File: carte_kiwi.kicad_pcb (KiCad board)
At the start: 2 copper layers, 50 x 50 mm, 44 parts, among them IC1 MCP2562, P1 CONN_01X05, P2 CONN_01X03, P3 CONN_01X05, P4 CONN_01X03, P5 Serial Wire, P6 CAN_conn, P7 CONN_01X03, P8 CONN_01X03, P9 CAN_conn, SW1 SW_Push, U1 LD1117S50TR, U2 LD1117S33TR, U3 STM32F303K8

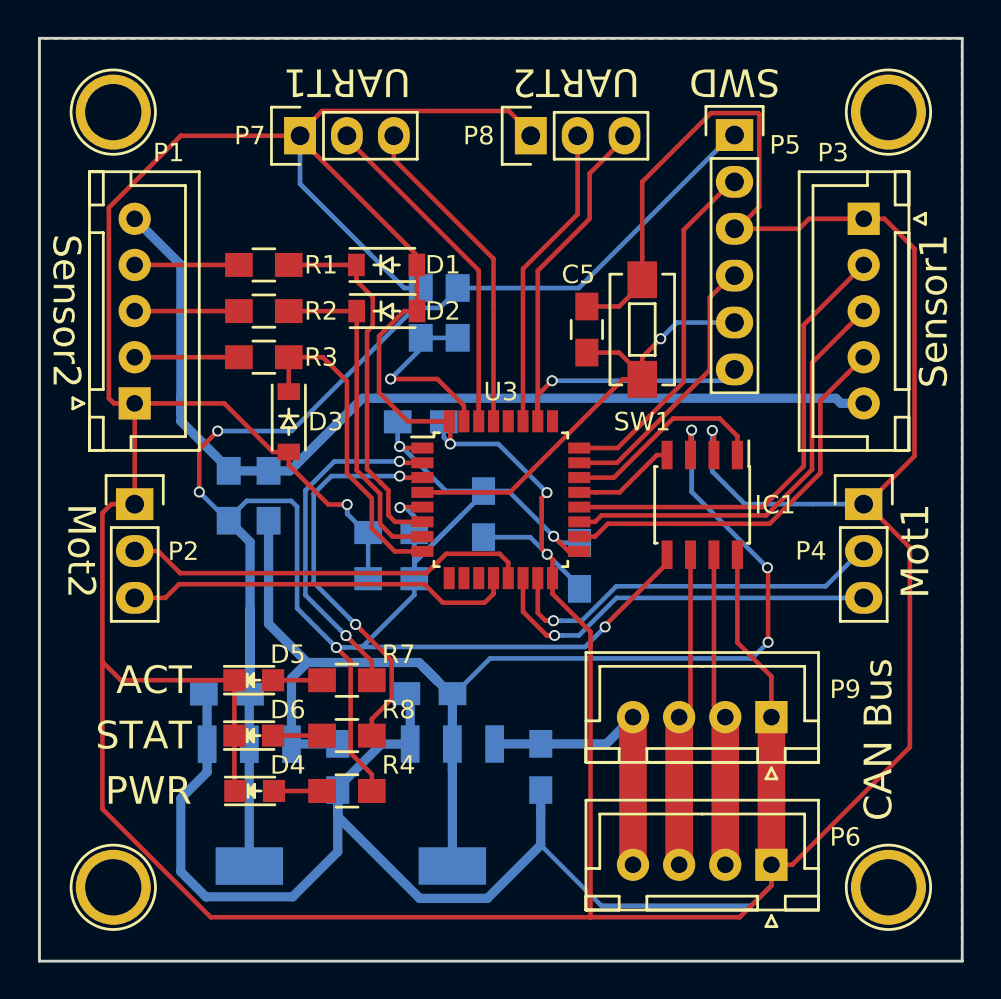
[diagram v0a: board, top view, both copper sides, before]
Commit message: ajoute via de connection entre plans de masse
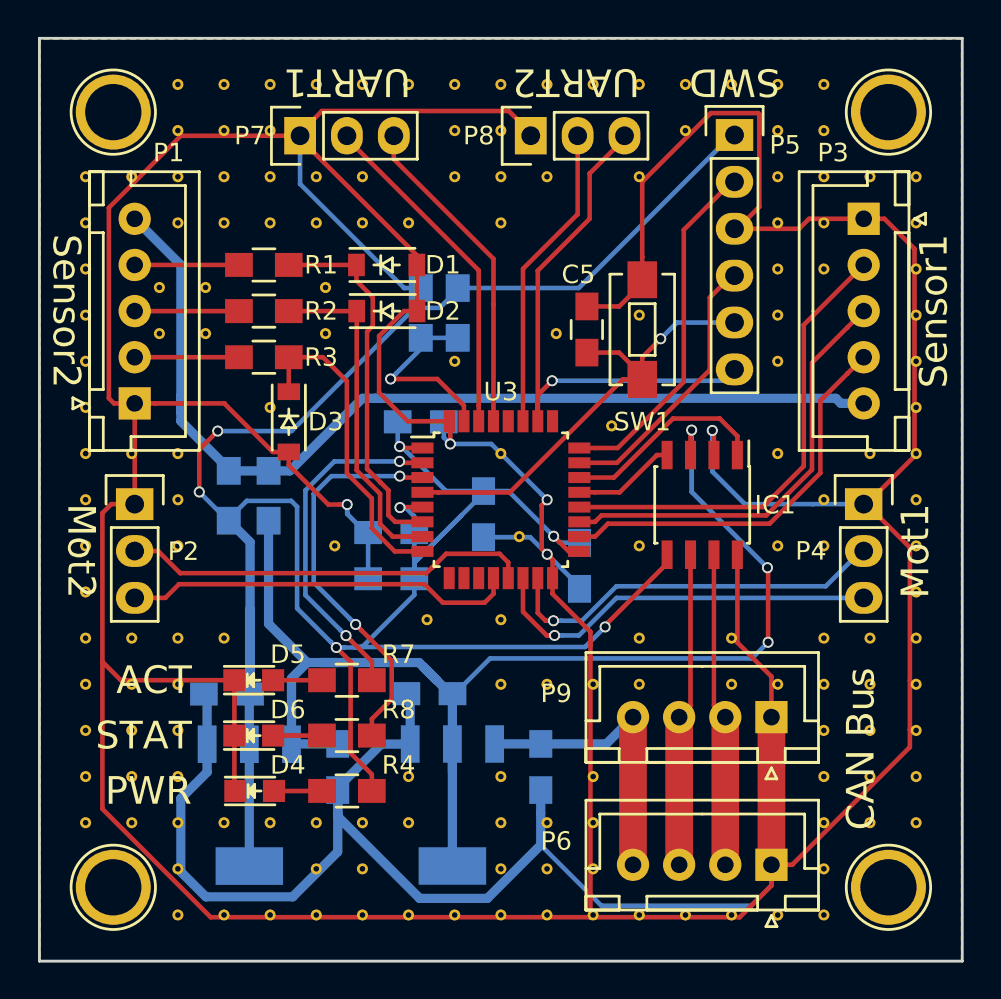
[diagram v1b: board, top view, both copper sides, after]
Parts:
- added REF**: Via, PhoenixRobotik:Via-0.6mm, F.Cu at (131.5, 101.0)
- added REF**: Via, PhoenixRobotik:Via-0.6mm, F.Cu at (140.5, 101.0)
- added REF**: Via, PhoenixRobotik:Via-0.6mm, F.Cu at (170.0, 107.5)
- added REF**: Via, PhoenixRobotik:Via-0.6mm, F.Cu at (165.0, 107.5)
- added REF**: Via, PhoenixRobotik:Via-0.6mm, F.Cu at (150.0, 107.5)
- added REF**: Via, PhoenixRobotik:Via-0.6mm, F.Cu at (132.5, 107.5)
- added REF**: Via, PhoenixRobotik:Via-0.6mm, F.Cu at (130.0, 107.5)
- added REF**: Via, PhoenixRobotik:Via-0.6mm, F.Cu at (127.5, 107.5)
- added REF**: Via, PhoenixRobotik:Via-0.6mm, F.Cu at (172.5, 105.0)
- added REF**: Via, PhoenixRobotik:Via-0.6mm, F.Cu at (137.5, 105.0)
- added REF**: Via, PhoenixRobotik:Via-0.6mm, F.Cu at (127.5, 105.0)
- added REF**: Via, PhoenixRobotik:Via-0.6mm, F.Cu at (172.5, 102.5)
- added REF**: Via, PhoenixRobotik:Via-0.6mm, F.Cu at (140.5, 98.5)
- added REF**: Via, PhoenixRobotik:Via-0.6mm, F.Cu at (165.0, 102.5)
- added REF**: Via, PhoenixRobotik:Via-0.6mm, F.Cu at (147.5, 102.5)
- added REF**: Via, PhoenixRobotik:Via-0.6mm, F.Cu at (127.5, 102.5)
- added REF**: Via, PhoenixRobotik:Via-0.6mm, F.Cu at (172.5, 100.0)
- added REF**: Via, PhoenixRobotik:Via-0.6mm, F.Cu at (165.0, 100.0)
- added REF**: Via, PhoenixRobotik:Via-0.6mm, F.Cu at (157.5, 100.0)
- added REF**: Via, PhoenixRobotik:Via-0.6mm, F.Cu at (127.5, 100.0)
- added REF**: Via, PhoenixRobotik:Via-0.6mm, F.Cu at (172.5, 97.5)
- added REF**: Via, PhoenixRobotik:Via-0.6mm, F.Cu at (167.5, 97.5)
- added REF**: Via, PhoenixRobotik:Via-0.6mm, F.Cu at (165.0, 97.5)
- added REF**: Via, PhoenixRobotik:Via-0.6mm, F.Cu at (157.5, 92.5)
- added REF**: Via, PhoenixRobotik:Via-0.6mm, F.Cu at (127.5, 97.5)
- added REF**: Via, PhoenixRobotik:Via-0.6mm, F.Cu at (172.5, 95.0)
- added REF**: Via, PhoenixRobotik:Via-0.6mm, F.Cu at (167.5, 95.0)
- added REF**: Via, PhoenixRobotik:Via-0.6mm, F.Cu at (165.0, 95.0)
- added REF**: Via, PhoenixRobotik:Via-0.6mm, F.Cu at (150.0, 95.0)
- added REF**: Via, PhoenixRobotik:Via-0.6mm, F.Cu at (145.0, 95.0)
- added REF**: Via, PhoenixRobotik:Via-0.6mm, F.Cu at (142.5, 95.0)
- added REF**: Via, PhoenixRobotik:Via-0.6mm, F.Cu at (140.0, 95.0)
- added REF**: Via, PhoenixRobotik:Via-0.6mm, F.Cu at (137.5, 95.0)
- added REF**: Via, PhoenixRobotik:Via-0.6mm, F.Cu at (135.0, 95.0)
- added REF**: Via, PhoenixRobotik:Via-0.6mm, F.Cu at (167.5, 132.5)
- added REF**: Via, PhoenixRobotik:Via-0.6mm, F.Cu at (132.5, 95.0)
- added REF**: Via, PhoenixRobotik:Via-0.6mm, F.Cu at (127.5, 95.0)
- added REF**: Via, PhoenixRobotik:Via-0.6mm, F.Cu at (172.5, 92.5)
- added REF**: Via, PhoenixRobotik:Via-0.6mm, F.Cu at (170.0, 92.5)
- added REF**: Via, PhoenixRobotik:Via-0.6mm, F.Cu at (167.5, 92.5)
- added REF**: Via, PhoenixRobotik:Via-0.6mm, F.Cu at (165.0, 92.5)
- added REF**: Via, PhoenixRobotik:Via-0.6mm, F.Cu at (152.5, 92.5)
- added REF**: Via, PhoenixRobotik:Via-0.6mm, F.Cu at (150.0, 92.5)
- added REF**: Via, PhoenixRobotik:Via-0.6mm, F.Cu at (147.5, 92.5)
- added REF**: Via, PhoenixRobotik:Via-0.6mm, F.Cu at (142.5, 92.5)
- added REF**: Via, PhoenixRobotik:Via-0.6mm, F.Cu at (165.0, 132.5)
- added REF**: Via, PhoenixRobotik:Via-0.6mm, F.Cu at (140.0, 92.5)
- added REF**: Via, PhoenixRobotik:Via-0.6mm, F.Cu at (137.5, 92.5)
- added REF**: Via, PhoenixRobotik:Via-0.6mm, F.Cu at (135.0, 92.5)
- added REF**: Via, PhoenixRobotik:Via-0.6mm, F.Cu at (132.5, 92.5)
- added REF**: Via, PhoenixRobotik:Via-0.6mm, F.Cu at (130.0, 92.5)
- added REF**: Via, PhoenixRobotik:Via-0.6mm, F.Cu at (127.5, 92.5)
- added REF**: Via, PhoenixRobotik:Via-0.6mm, F.Cu at (167.5, 90.0)
- added REF**: Via, PhoenixRobotik:Via-0.6mm, F.Cu at (165.0, 90.0)
- added REF**: Via, PhoenixRobotik:Via-0.6mm, F.Cu at (160.0, 90.0)
- added REF**: Via, PhoenixRobotik:Via-0.6mm, F.Cu at (150.0, 90.0)
- added REF**: Via, PhoenixRobotik:Via-0.6mm, F.Cu at (162.5, 132.5)
- added REF**: Via, PhoenixRobotik:Via-0.6mm, F.Cu at (147.5, 90.0)
- added REF**: Via, PhoenixRobotik:Via-0.6mm, F.Cu at (137.5, 90.0)
- added REF**: Via, PhoenixRobotik:Via-0.6mm, F.Cu at (135.0, 90.0)
- added REF**: Via, PhoenixRobotik:Via-0.6mm, F.Cu at (132.5, 90.0)
- added REF**: Via, PhoenixRobotik:Via-0.6mm, F.Cu at (167.5, 87.5)
- added REF**: Via, PhoenixRobotik:Via-0.6mm, F.Cu at (165.0, 87.5)
- added REF**: Via, PhoenixRobotik:Via-0.6mm, F.Cu at (162.5, 87.5)
- added REF**: Via, PhoenixRobotik:Via-0.6mm, F.Cu at (160.0, 87.5)
- added REF**: Via, PhoenixRobotik:Via-0.6mm, F.Cu at (157.5, 87.5)
- added REF**: Via, PhoenixRobotik:Via-0.6mm, F.Cu at (155.0, 87.5)
- added REF**: Via, PhoenixRobotik:Via-0.6mm, F.Cu at (160.0, 132.5)
- added REF**: Via, PhoenixRobotik:Via-0.6mm, F.Cu at (152.5, 87.5)
- added REF**: Via, PhoenixRobotik:Via-0.6mm, F.Cu at (150.0, 87.5)
- added REF**: Via, PhoenixRobotik:Via-0.6mm, F.Cu at (147.5, 87.5)
- added REF**: Via, PhoenixRobotik:Via-0.6mm, F.Cu at (145.0, 87.5)
- added REF**: Via, PhoenixRobotik:Via-0.6mm, F.Cu at (142.5, 87.5)
- added REF**: Via, PhoenixRobotik:Via-0.6mm, F.Cu at (140.0, 87.5)
- added REF**: Via, PhoenixRobotik:Via-0.6mm, F.Cu at (137.5, 87.5)
- added REF**: Via, PhoenixRobotik:Via-0.6mm, F.Cu at (135.0, 87.5)
- added REF**: Via, PhoenixRobotik:Via-0.6mm, F.Cu at (132.5, 87.5)
- added REF**: Via, PhoenixRobotik:Via-0.6mm, F.Cu at (157.5, 132.5)
- added REF**: Via, PhoenixRobotik:Via-0.6mm, F.Cu at (155.0, 132.5)
- added REF**: Via, PhoenixRobotik:Via-0.6mm, F.Cu at (152.5, 132.5)
- added REF**: Via, PhoenixRobotik:Via-0.6mm, F.Cu at (131.5, 98.5)
- added REF**: Via, PhoenixRobotik:Via-0.6mm, F.Cu at (150.0, 132.5)
- added REF**: Via, PhoenixRobotik:Via-0.6mm, F.Cu at (147.5, 132.5)
- added REF**: Via, PhoenixRobotik:Via-0.6mm, F.Cu at (145.0, 132.5)
- added REF**: Via, PhoenixRobotik:Via-0.6mm, F.Cu at (142.5, 132.5)
- added REF**: Via, PhoenixRobotik:Via-0.6mm, F.Cu at (140.0, 132.5)
- added REF**: Via, PhoenixRobotik:Via-0.6mm, F.Cu at (137.5, 132.5)
- added REF**: Via, PhoenixRobotik:Via-0.6mm, F.Cu at (135.0, 132.5)
- added REF**: Via, PhoenixRobotik:Via-0.6mm, F.Cu at (132.5, 132.5)
- added REF**: Via, PhoenixRobotik:Via-0.6mm, F.Cu at (167.5, 130.0)
- added REF**: Via, PhoenixRobotik:Via-0.6mm, F.Cu at (155.0, 130.0)
- added REF**: Via, PhoenixRobotik:Via-0.6mm, F.Cu at (134.0, 101.0)
- added REF**: Via, PhoenixRobotik:Via-0.6mm, F.Cu at (152.5, 130.0)
- added REF**: Via, PhoenixRobotik:Via-0.6mm, F.Cu at (150.0, 130.0)
- added REF**: Via, PhoenixRobotik:Via-0.6mm, F.Cu at (142.5, 130.0)
- added REF**: Via, PhoenixRobotik:Via-0.6mm, F.Cu at (140.0, 130.0)
- added REF**: Via, PhoenixRobotik:Via-0.6mm, F.Cu at (132.5, 130.0)
- added REF**: Via, PhoenixRobotik:Via-0.6mm, F.Cu at (172.5, 127.5)
- added REF**: Via, PhoenixRobotik:Via-0.6mm, F.Cu at (170.0, 127.5)
- added REF**: Via, PhoenixRobotik:Via-0.6mm, F.Cu at (167.5, 127.5)
- added REF**: Via, PhoenixRobotik:Via-0.6mm, F.Cu at (155.0, 127.5)
- added REF**: Via, PhoenixRobotik:Via-0.6mm, F.Cu at (152.5, 127.5)
- added REF**: Via, PhoenixRobotik:Via-0.6mm, F.Cu at (134.0, 98.5)
- added REF**: Via, PhoenixRobotik:Via-0.6mm, F.Cu at (150.0, 127.5)
- added REF**: Via, PhoenixRobotik:Via-0.6mm, F.Cu at (145.0, 127.5)
- added REF**: Via, PhoenixRobotik:Via-0.6mm, F.Cu at (142.5, 127.5)
- added REF**: Via, PhoenixRobotik:Via-0.6mm, F.Cu at (140.0, 127.5)
- added REF**: Via, PhoenixRobotik:Via-0.6mm, F.Cu at (137.5, 127.5)
- added REF**: Via, PhoenixRobotik:Via-0.6mm, F.Cu at (135.0, 127.5)
- added REF**: Via, PhoenixRobotik:Via-0.6mm, F.Cu at (132.5, 127.5)
- added REF**: Via, PhoenixRobotik:Via-0.6mm, F.Cu at (130.0, 127.5)
- added REF**: Via, PhoenixRobotik:Via-0.6mm, F.Cu at (127.5, 127.5)
- added REF**: Via, PhoenixRobotik:Via-0.6mm, F.Cu at (172.5, 125.0)
- added REF**: Via, PhoenixRobotik:Via-0.6mm, F.Cu at (156.0, 106.0)
- added REF**: Via, PhoenixRobotik:Via-0.6mm, F.Cu at (170.0, 125.0)
- added REF**: Via, PhoenixRobotik:Via-0.6mm, F.Cu at (167.5, 125.0)
- added REF**: Via, PhoenixRobotik:Via-0.6mm, F.Cu at (155.0, 125.0)
- added REF**: Via, PhoenixRobotik:Via-0.6mm, F.Cu at (150.0, 125.0)
- added REF**: Via, PhoenixRobotik:Via-0.6mm, F.Cu at (145.0, 125.0)
- added REF**: Via, PhoenixRobotik:Via-0.6mm, F.Cu at (132.5, 125.0)
- added REF**: Via, PhoenixRobotik:Via-0.6mm, F.Cu at (130.0, 125.0)
- added REF**: Via, PhoenixRobotik:Via-0.6mm, F.Cu at (127.5, 125.0)
- added REF**: Via, PhoenixRobotik:Via-0.6mm, F.Cu at (172.5, 122.5)
- added REF**: Via, PhoenixRobotik:Via-0.6mm, F.Cu at (170.0, 122.5)
- added REF**: Via, PhoenixRobotik:Via-0.6mm, F.Cu at (150.0, 116.5)
- added REF**: Via, PhoenixRobotik:Via-0.6mm, F.Cu at (167.5, 122.5)
- added REF**: Via, PhoenixRobotik:Via-0.6mm, F.Cu at (132.5, 122.5)
- added REF**: Via, PhoenixRobotik:Via-0.6mm, F.Cu at (130.0, 122.5)
- added REF**: Via, PhoenixRobotik:Via-0.6mm, F.Cu at (127.5, 122.5)
- added REF**: Via, PhoenixRobotik:Via-0.6mm, F.Cu at (172.5, 120.0)
- added REF**: Via, PhoenixRobotik:Via-0.6mm, F.Cu at (170.0, 120.0)
- added REF**: Via, PhoenixRobotik:Via-0.6mm, F.Cu at (167.5, 120.0)
- added REF**: Via, PhoenixRobotik:Via-0.6mm, F.Cu at (165.0, 120.0)
- added REF**: Via, PhoenixRobotik:Via-0.6mm, F.Cu at (162.5, 120.0)
- added REF**: Via, PhoenixRobotik:Via-0.6mm, F.Cu at (157.5, 120.0)
- added REF**: Via, PhoenixRobotik:Via-0.6mm, F.Cu at (151.0, 112.0)
- added REF**: Via, PhoenixRobotik:Via-0.6mm, F.Cu at (155.0, 120.0)
- added REF**: Via, PhoenixRobotik:Via-0.6mm, F.Cu at (152.5, 120.0)
- added REF**: Via, PhoenixRobotik:Via-0.6mm, F.Cu at (150.0, 120.0)
- added REF**: Via, PhoenixRobotik:Via-0.6mm, F.Cu at (132.5, 120.0)
- added REF**: Via, PhoenixRobotik:Via-0.6mm, F.Cu at (130.0, 120.0)
- added REF**: Via, PhoenixRobotik:Via-0.6mm, F.Cu at (127.5, 120.0)
- added REF**: Via, PhoenixRobotik:Via-0.6mm, F.Cu at (172.5, 117.5)
- added REF**: Via, PhoenixRobotik:Via-0.6mm, F.Cu at (170.0, 117.5)
- added REF**: Via, PhoenixRobotik:Via-0.6mm, F.Cu at (167.5, 117.5)
- added REF**: Via, PhoenixRobotik:Via-0.6mm, F.Cu at (162.5, 117.5)
- added REF**: Via, PhoenixRobotik:Via-0.6mm, F.Cu at (146.0, 116.5)
- added REF**: Via, PhoenixRobotik:Via-0.6mm, F.Cu at (157.5, 117.5)
- added REF**: Via, PhoenixRobotik:Via-0.6mm, F.Cu at (135.0, 117.5)
- added REF**: Via, PhoenixRobotik:Via-0.6mm, F.Cu at (132.5, 117.5)
- added REF**: Via, PhoenixRobotik:Via-0.6mm, F.Cu at (130.0, 117.5)
- added REF**: Via, PhoenixRobotik:Via-0.6mm, F.Cu at (127.5, 117.5)
- added REF**: Via, PhoenixRobotik:Via-0.6mm, F.Cu at (172.5, 115.0)
- added REF**: Via, PhoenixRobotik:Via-0.6mm, F.Cu at (127.5, 115.0)
- added REF**: Via, PhoenixRobotik:Via-0.6mm, F.Cu at (172.5, 112.5)
- added REF**: Via, PhoenixRobotik:Via-0.6mm, F.Cu at (167.5, 112.5)
- added REF**: Via, PhoenixRobotik:Via-0.6mm, F.Cu at (165.0, 112.5)
- added REF**: Via, PhoenixRobotik:Via-0.6mm, F.Cu at (153.0, 101.0)
- added REF**: Via, PhoenixRobotik:Via-0.6mm, F.Cu at (157.5, 112.5)
- added REF**: Via, PhoenixRobotik:Via-0.6mm, F.Cu at (141.0, 112.5)
- added REF**: Via, PhoenixRobotik:Via-0.6mm, F.Cu at (132.5, 112.5)
- added REF**: Via, PhoenixRobotik:Via-0.6mm, F.Cu at (127.5, 112.5)
- added REF**: Via, PhoenixRobotik:Via-0.6mm, F.Cu at (172.5, 110.0)
- added REF**: Via, PhoenixRobotik:Via-0.6mm, F.Cu at (167.5, 110.0)
- added REF**: Via, PhoenixRobotik:Via-0.6mm, F.Cu at (132.5, 110.0)
- added REF**: Via, PhoenixRobotik:Via-0.6mm, F.Cu at (130.0, 110.0)
- added REF**: Via, PhoenixRobotik:Via-0.6mm, F.Cu at (127.5, 110.0)
- added REF**: Via, PhoenixRobotik:Via-0.6mm, F.Cu at (172.5, 107.5)

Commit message: add test points on unused pins
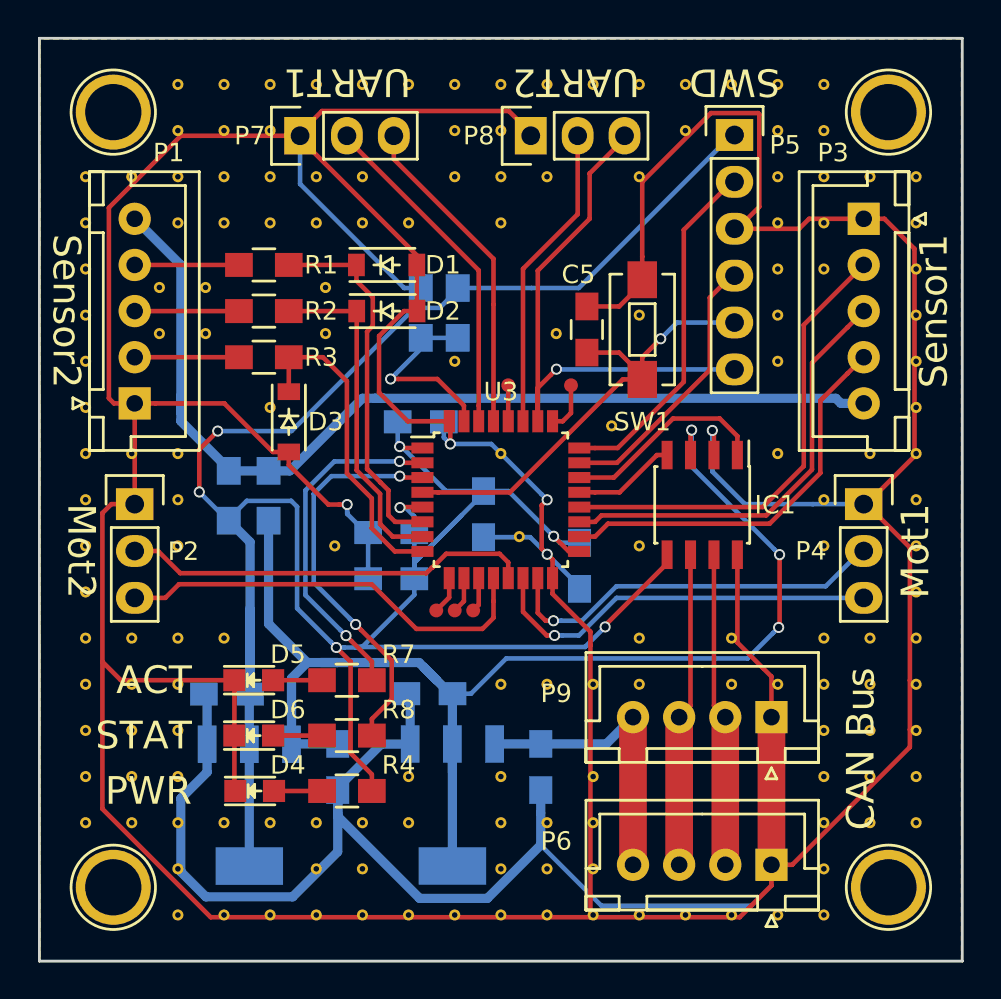
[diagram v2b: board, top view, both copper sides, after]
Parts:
- removed the REF** at (150.0, 116.5)
- removed the REF** at (146.0, 116.5)
- removed the REF** at (165.0, 112.5)
- added REF**: TestPoint, PhoenixRobotik:TestPoint, F.Cu at (150.4, 103.8)
- added REF**: TestPoint, PhoenixRobotik:TestPoint, F.Cu at (146.5, 116.0)
- added REF**: TestPoint, PhoenixRobotik:TestPoint, F.Cu at (153.8, 103.8)
- added REF**: TestPoint, PhoenixRobotik:TestPoint, F.Cu at (148.5, 116.0)
- added REF**: TestPoint, PhoenixRobotik:TestPoint, F.Cu at (147.5, 116.0)
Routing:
- net (no net): track 0.00 -> 10.5 mm
- net TIM3|PWM1: track 21.2 -> 23.1 mm

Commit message: améliore un peu ?
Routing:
- net +5V: track 70.3 -> 74.5 mm
- net GND: track 376.6 -> 374.1 mm
- net CAN_TX: track 11.3 -> 10.7 mm

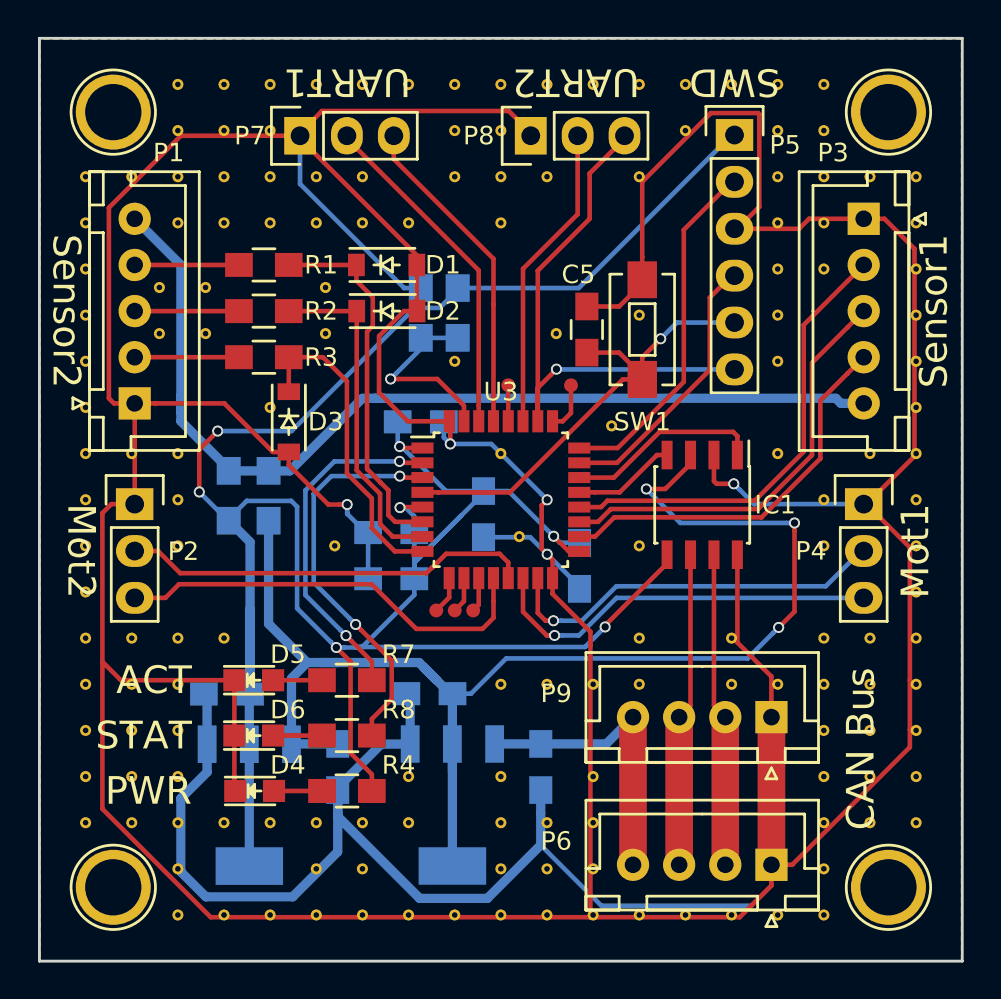
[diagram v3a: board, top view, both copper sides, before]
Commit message: bouge le transceiver CAN pour simplifier le routage
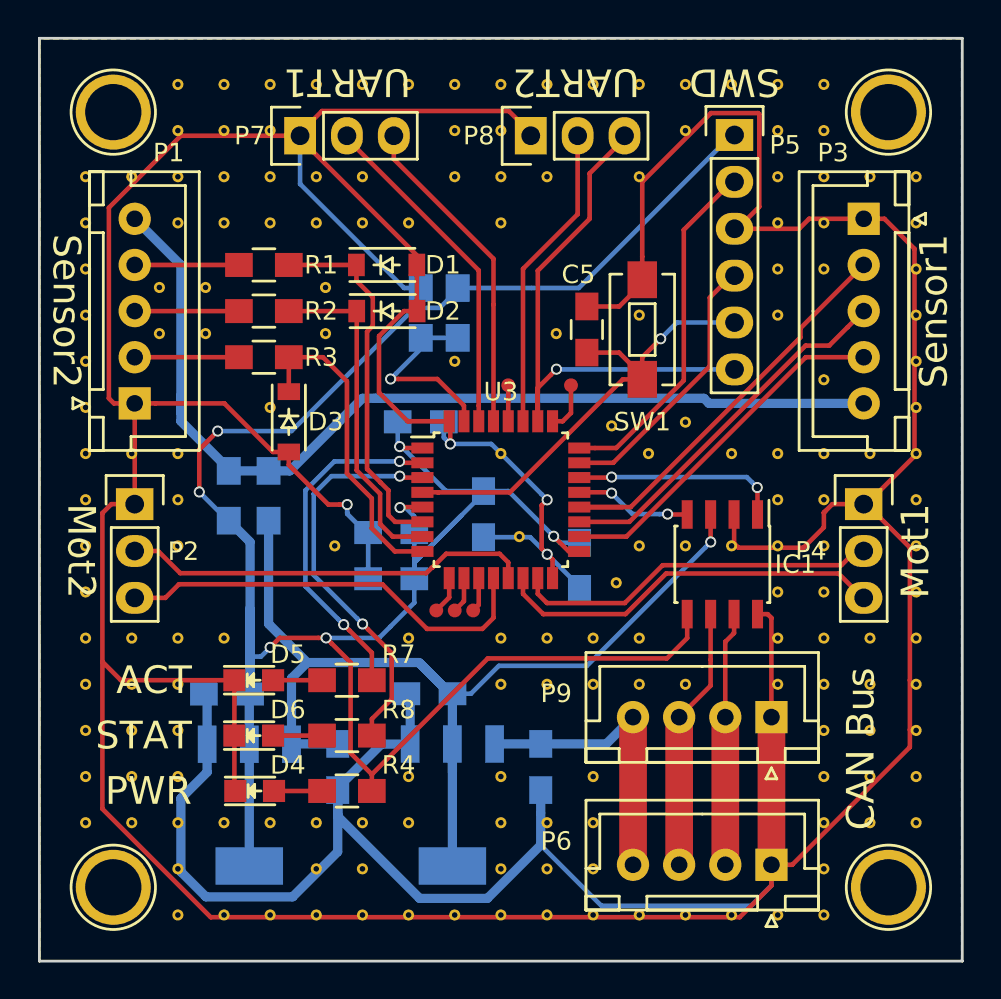
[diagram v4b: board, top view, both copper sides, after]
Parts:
- removed the REF** at (165.0, 102.5)
- removed the REF** at (162.5, 120.0)
- removed the REF** at (162.5, 117.5)
- added REF**: Via, PhoenixRobotik:Via-0.6mm, F.Cu at (167.5, 103.5)
- added REF**: Via, PhoenixRobotik:Via-0.6mm, F.Cu at (145.0, 117.5)
- added REF**: Via, PhoenixRobotik:Via-0.6mm, F.Cu at (150.0, 117.5)
- added REF**: Via, PhoenixRobotik:Via-0.6mm, F.Cu at (152.5, 117.5)
- added REF**: Via, PhoenixRobotik:Via-0.6mm, F.Cu at (155.0, 117.5)
- added REF**: Via, PhoenixRobotik:Via-0.6mm, F.Cu at (160.0, 112.5)
- added REF**: Via, PhoenixRobotik:Via-0.6mm, F.Cu at (162.5, 107.5)
- added REF**: Via, PhoenixRobotik:Via-0.6mm, F.Cu at (160.0, 105.8)
- added REF**: Via, PhoenixRobotik:Via-0.6mm, F.Cu at (165.0, 110.0)
- added REF**: Via, PhoenixRobotik:Via-0.6mm, F.Cu at (167.5, 107.5)
- added REF**: Via, PhoenixRobotik:Via-0.6mm, F.Cu at (158.0, 107.5)
- added REF**: Via, PhoenixRobotik:Via-0.6mm, F.Cu at (165.0, 117.5)
- added REF**: Via, PhoenixRobotik:Via-0.6mm, F.Cu at (160.0, 120.0)
- added REF**: Via, PhoenixRobotik:Via-0.6mm, F.Cu at (156.2, 114.5)
- added REF**: Via, PhoenixRobotik:Via-0.6mm, F.Cu at (162.5, 112.5)
- added REF**: Via, PhoenixRobotik:Via-0.6mm, F.Cu at (165.0, 112.5)
- added REF**: Via, PhoenixRobotik:Via-0.6mm, F.Cu at (165.0, 115.0)
- added REF**: Via, PhoenixRobotik:Via-0.6mm, F.Cu at (167.5, 115.0)
- moved IC1 3.40 mm to (162.0, 113.5)
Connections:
- REF** pad 1: (no net) -> Net-(U3-Pad9)
- REF** pad 1: (no net) -> Net-(U3-Pad28)
- REF** pad 1: (no net) -> Net-(U3-Pad25)
- REF** pad 1: (no net) -> Net-(U3-Pad11)
- REF** pad 1: (no net) -> Net-(U3-Pad10)
- U3 pad 10: (no net) -> Net-(U3-Pad10)
- U3 pad 11: (no net) -> Net-(U3-Pad11)
- U3 pad 25: (no net) -> Net-(U3-Pad25)
- U3 pad 28: (no net) -> Net-(U3-Pad28)
- U3 pad 9: (no net) -> Net-(U3-Pad9)
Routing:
- net GND: track 374.1 -> 351.8 mm, vias 5 -> 4
- net +5V: track 74.5 -> 57.5 mm, vias 3 -> 1
- net (no net): track 10.5 -> 0.00 mm
- net +3V3: track 143.3 -> 138.7 mm
- net CAN_H: track 17.1 -> 13.8 mm
- net TIM1|ENCB/Hall2: track 23.1 -> 20.1 mm
- net CAN_L: track 17.1 -> 14.3 mm
- net Net-(U3-Pad25): track 0.00 -> 2.69 mm
- net Net-(U3-Pad9): track 0.00 -> 2.04 mm
- net Net-(U3-Pad10): track 0.00 -> 1.96 mm
- net Net-(U3-Pad28): track 0.00 -> 1.95 mm
- net Net-(U3-Pad11): track 0.00 -> 1.87 mm
- net TIM1|ENCA/Hall1: track 21.3 -> 19.4 mm
- net TIM1|Hall3: track 24.9 -> 23.5 mm
- net TIM3|DIR2/PWM4: track 21.3 -> 20.0 mm, vias 1 -> 0
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
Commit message: ameliore masse
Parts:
- removed the REF** at (141.0, 112.5)
- added REF**: Via, PhoenixRobotik:Via-0.6mm, F.Cu at (155.0, 97.5)
- added REF**: Via, PhoenixRobotik:Via-0.6mm, F.Cu at (160.0, 92.5)
- added REF**: Via, PhoenixRobotik:Via-0.6mm, F.Cu at (152.5, 95.0)
- added REF**: Via, PhoenixRobotik:Via-0.6mm, F.Cu at (157.5, 95.0)
- added REF**: Via, PhoenixRobotik:Via-0.6mm, F.Cu at (155.0, 95.0)
- added REF**: Via, PhoenixRobotik:Via-0.6mm, F.Cu at (160.0, 97.5)
- added REF**: Via, PhoenixRobotik:Via-0.6mm, F.Cu at (160.0, 95.0)
- added REF**: Via, PhoenixRobotik:Via-0.6mm, F.Cu at (160.0, 100.0)
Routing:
- net GND: track 351.8 -> 363.6 mm
- net SWCLK: track 19.2 -> 20.1 mm
- net Sensor_PWR: track 53.3 -> 54.0 mm
